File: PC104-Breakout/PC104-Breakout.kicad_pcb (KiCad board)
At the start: 4 copper layers, 175 x 100 mm, 20 parts, among them J1 Screw_Terminal_01x02, J2 Screw_Terminal_01x02, J3 Screw_Terminal_01x02, M1 MountingHole_Pad, M2 MountingHole_Pad, M3 MountingHole_Pad, M4 MountingHole_Pad, M5 MountingHole_Pad, M6 MountingHole_Pad, M7 MountingHole_Pad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

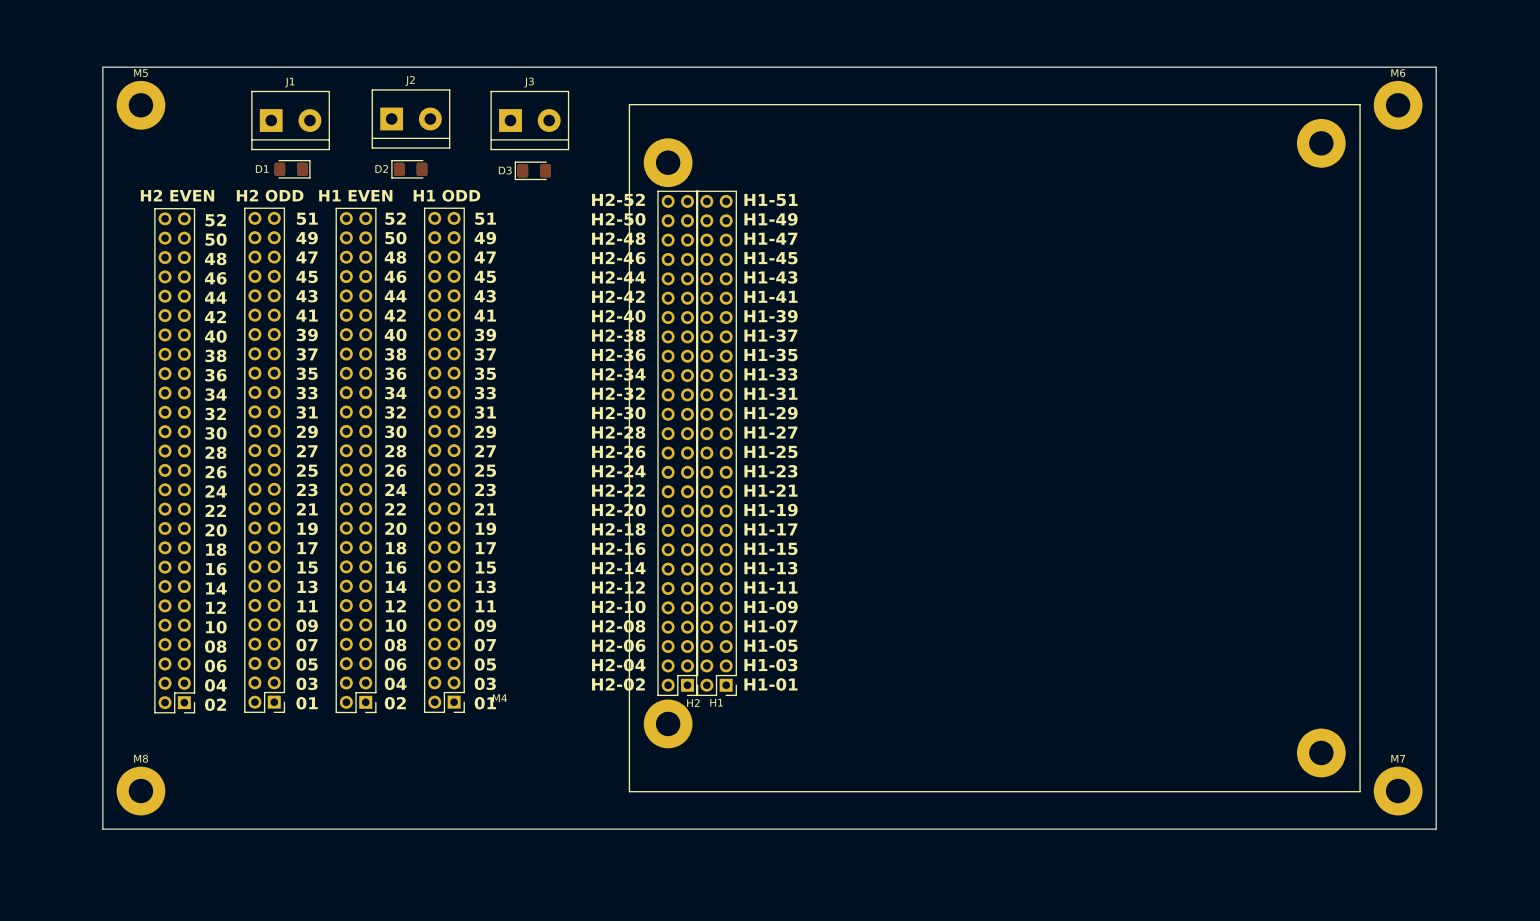
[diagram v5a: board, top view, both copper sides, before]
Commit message: semi final routing
- routed everything including power pins
- created GND, 3V3, and 5V pours
- added vias for diodes / routing

TODO: fix last two unrouted nets
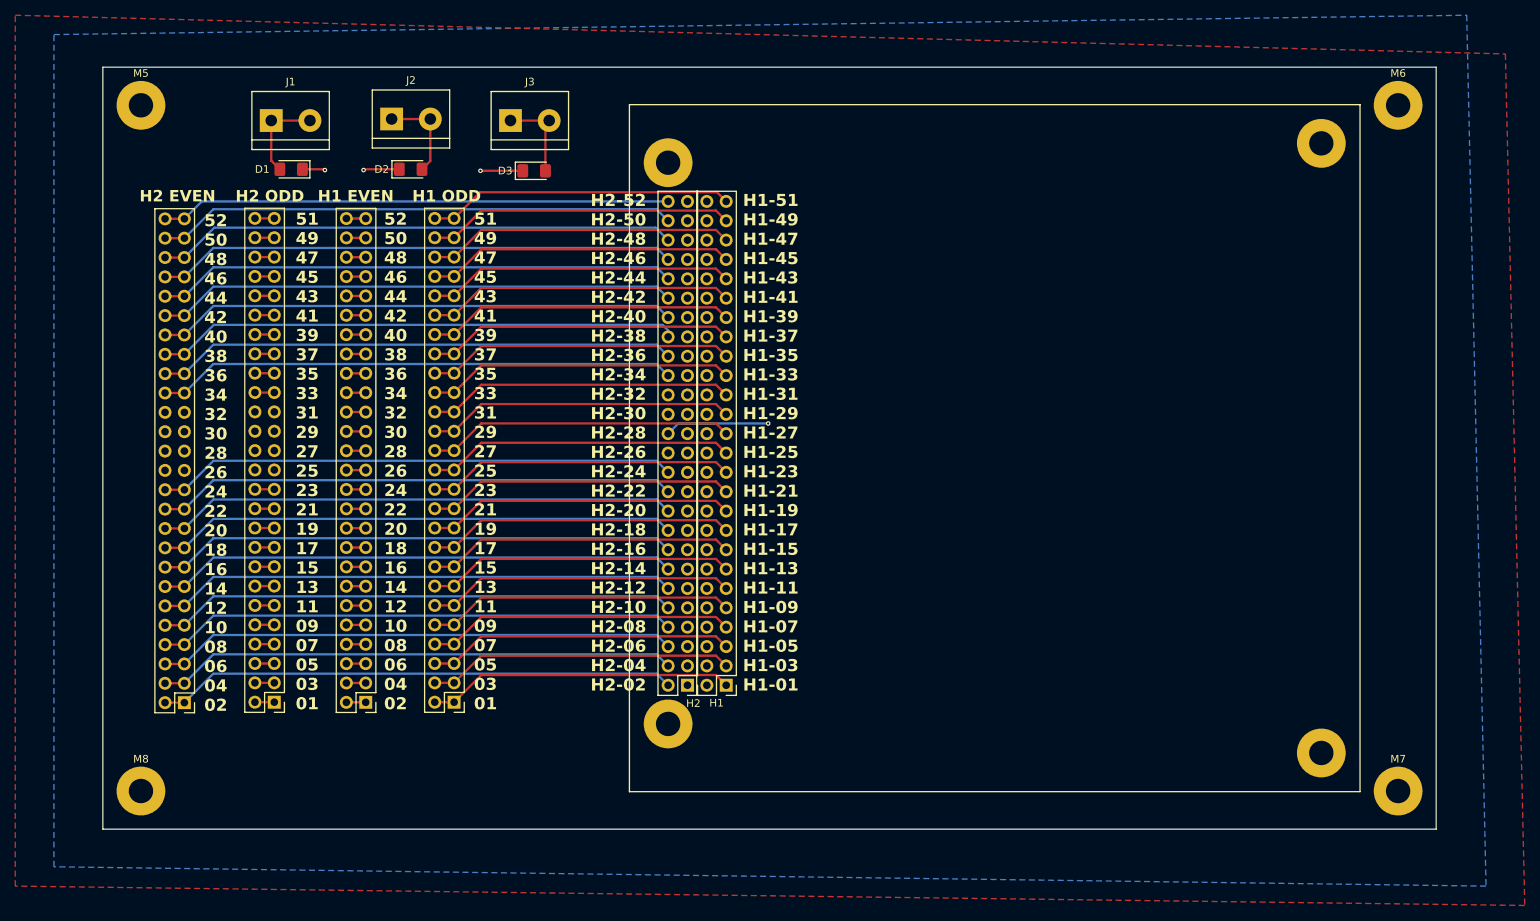
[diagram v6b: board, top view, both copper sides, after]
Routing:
- net H2-38: track 0.00 -> 68.8 mm
- net H2-48: track 0.00 -> 68.3 mm
- net H2-34: track 0.00 -> 68.2 mm
- net H2-20: track 0.00 -> 68.2 mm
- net H2-16: track 0.00 -> 68.2 mm
- net H2-02: track 0.00 -> 68.2 mm
- net H2-50: track 0.00 -> 68.2 mm
- net H2-46: track 0.00 -> 68.2 mm
- net H2-44: track 0.00 -> 68.2 mm
- net H2-42: track 0.00 -> 68.2 mm
- net H2-40: track 0.00 -> 68.2 mm
- net H2-36: track 0.00 -> 68.2 mm
- net H2-24: track 0.00 -> 68.2 mm
- net H2-22: track 0.00 -> 68.2 mm
- net H2-18: track 0.00 -> 68.2 mm
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- added copper zone on F.Cu, net H2-25
- added copper zone on In1.Cu, net H2-27
- added copper zone on B.Cu, net H2-29

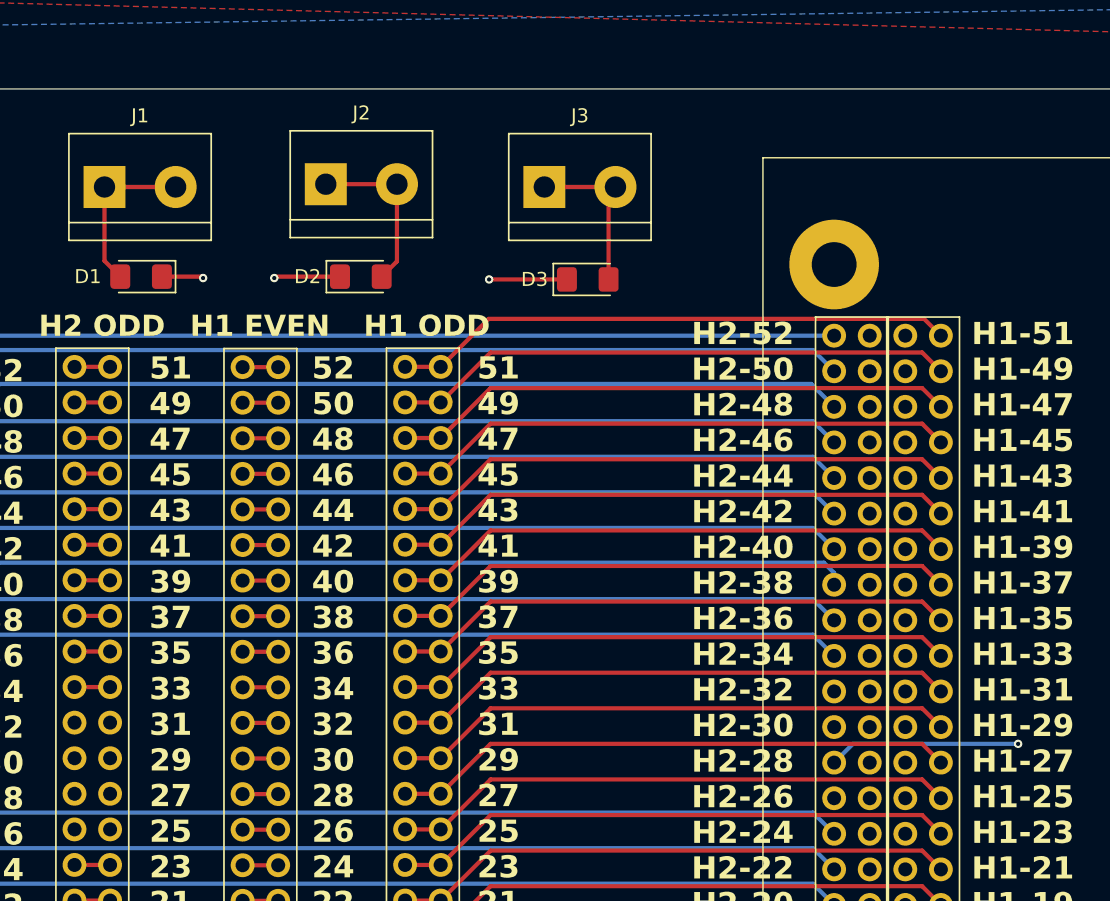
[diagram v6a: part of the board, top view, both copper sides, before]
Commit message: finished routing
- fixed final unrouted nets and vias
- silk screen edits
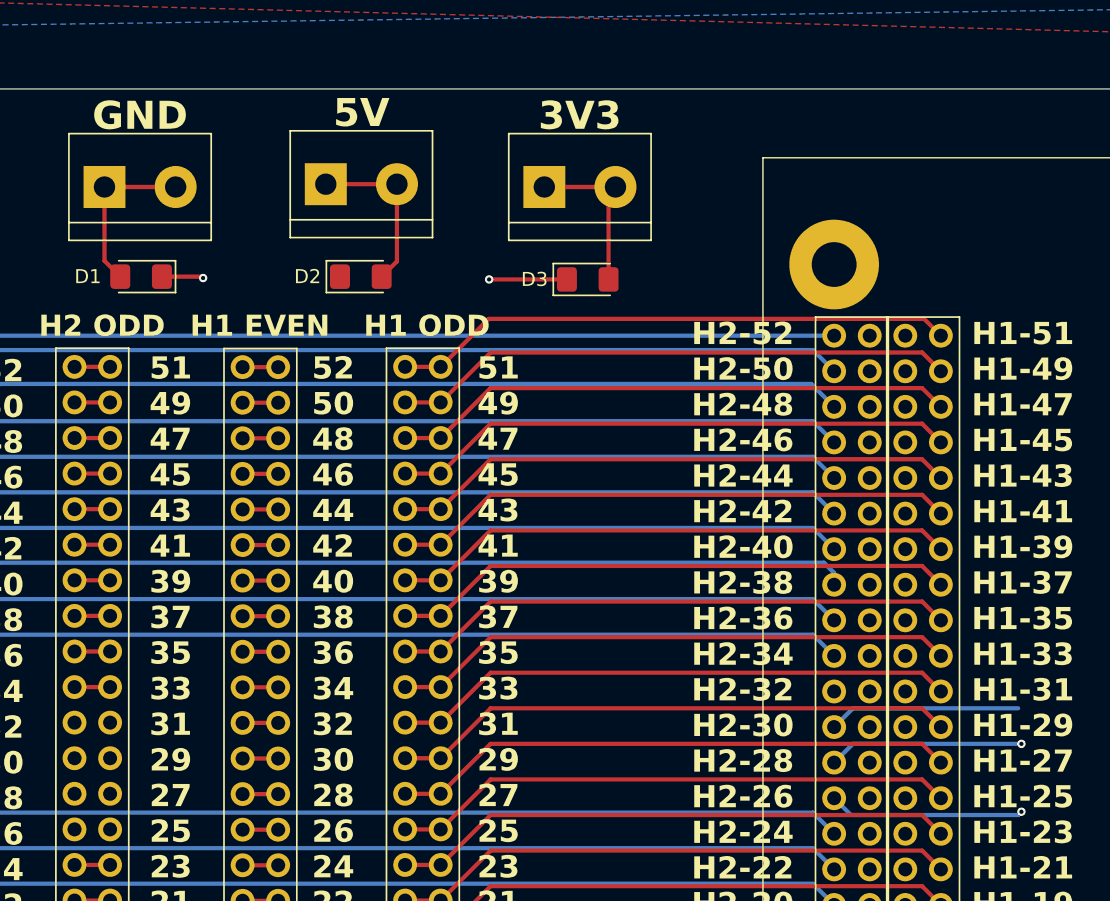
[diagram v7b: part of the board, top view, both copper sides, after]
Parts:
- renumbered J3 to 3V3, J2 to 5V, J1 to GND
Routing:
- net H2-29: track 3.15 -> 16.8 mm
- net H2-25: track 4.73 -> 14.0 mm
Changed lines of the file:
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@@
 		(descr "simple 2-pin terminal block, pitch 5.08mm, revamped version of bornier2")
 		(tags "terminal block bornier2")
-		(property "Reference" "J1"
+		(property "Reference" "GND"
 			(at 2.54 -5.08 0)
 			(layer "F.SilkS")
 			(effects
 				(font
-					(size 1 1)
-					(thickness 0.15)
+					(size 2 2)
+					(thickness 0.4)
+					(bold yes)
 				)
 			)
@@
 		(descr "simple 2-pin terminal block, pitch 5.08mm, revamped version of bornier2")
 		(tags "terminal block bornier2")
-		(property "Reference" "J3"
+		(property "Reference" "3V3"
 			(at 2.54 -5.08 0)
 			(layer "F.SilkS")
 			(effects
 				(font
-					(size 1 1)
-					(thickness 0.15)
+					(size 2 2)
+					(thickness 0.4)
+					(bold yes)
 				)
 			)
@@
 		(descr "simple 2-pin terminal block, pitch 5.08mm, revamped version of bornier2")
 		(tags "terminal block bornier2")
-		(property "Reference" "J2"
+		(property "Reference" "5V"
 			(at 2.54 -5.08 0)
 			(layer "F.SilkS")
 			(effects
 				(font
-					(size 1 1)
-					(thickness 0.15)
+					(size 2 2)
+					(thickness 0.4)
+					(bold yes)
 				)
 			)
@@
 		(net 55)
 	)
+	(via
+		(at 162.56 101.6)
+		(size 0.6)
+		(drill 0.3)
+		(layers "F.Cu" "B.Cu")
+		(net 56)
+	)
 	(segment
-		(start 113.9125 63.4)
-		(end 109.32 63.4)
+		(start 150.39 101.835)
+		(end 162.325 101.835)
 		(width 0.3)
-		(layer "F.Cu")
+		(layer "B.Cu")
 		(net 56)
 	)
 	(segment
-		(start 109.32 63.4)
-		(end 109.22 63.5)
+		(start 149.19 100.635)
+		(end 150.39 101.835)
 		(width 0.3)
-		(layer "F.Cu")
+		(layer "B.Cu")
 		(net 56)
 	)
-	(via
-		(at 109.22 63.5)
-		(size 0.6)
-		(drill 0.3)
-		(layers "F.Cu" "B.Cu")
+	(segment
+		(start 162.325 101.835)
+		(end 162.56 101.6)
+		(width 0.3)
+		(layer "B.Cu")
 		(net 56)
 	)
@@
 	)
 	(segment
+		(start 150.53 94.215)
+		(end 162.325 94.215)
+		(width 0.3)
+		(layer "B.Cu")
+		(net 58)
+	)
+	(segment
+		(start 149.19 95.555)
+		(end 150.53 94.215)
+		(width 0.3)
+		(layer "B.Cu")
+		(net 58)
+	)
+	(segment
 		(start 94.96 92.7)
 		(end 97.5 92.7)
@@
 	)
 	(via
-		(at 162.325 96.755)
+		(at 162.56 96.755)
 		(size 0.6)
 		(drill 0.3)
@@
 	)
 	(segment
-		(start 162.325 96.755)
+		(start 149.19 98.095)
 		(end 150.53 96.755)
 		(width 0.3)
@@
 	(segment
 		(start 150.53 96.755)
-		(end 149.19 98.095)
+		(end 162.56 96.755)
 		(width 0.3)
 		(layer "B.Cu")

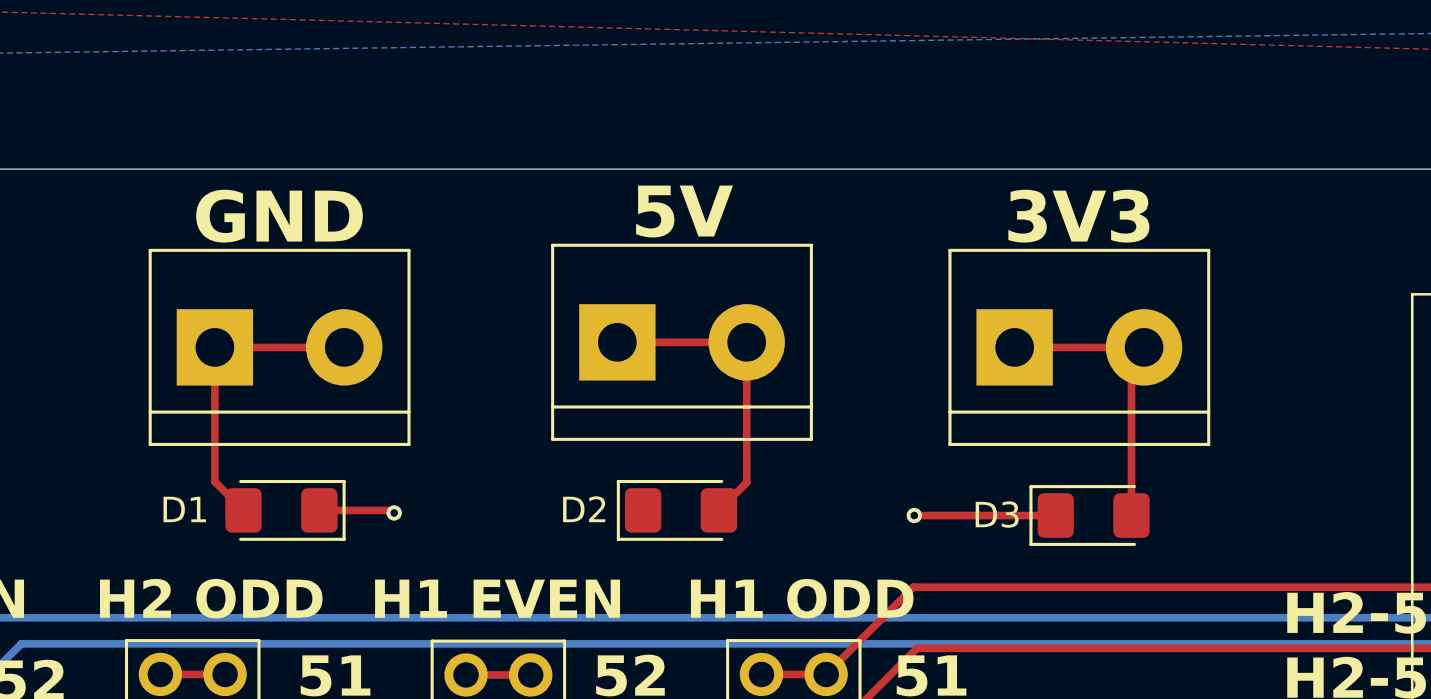
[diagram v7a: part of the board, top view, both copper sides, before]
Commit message: Fixed LED orientations and finalized board design
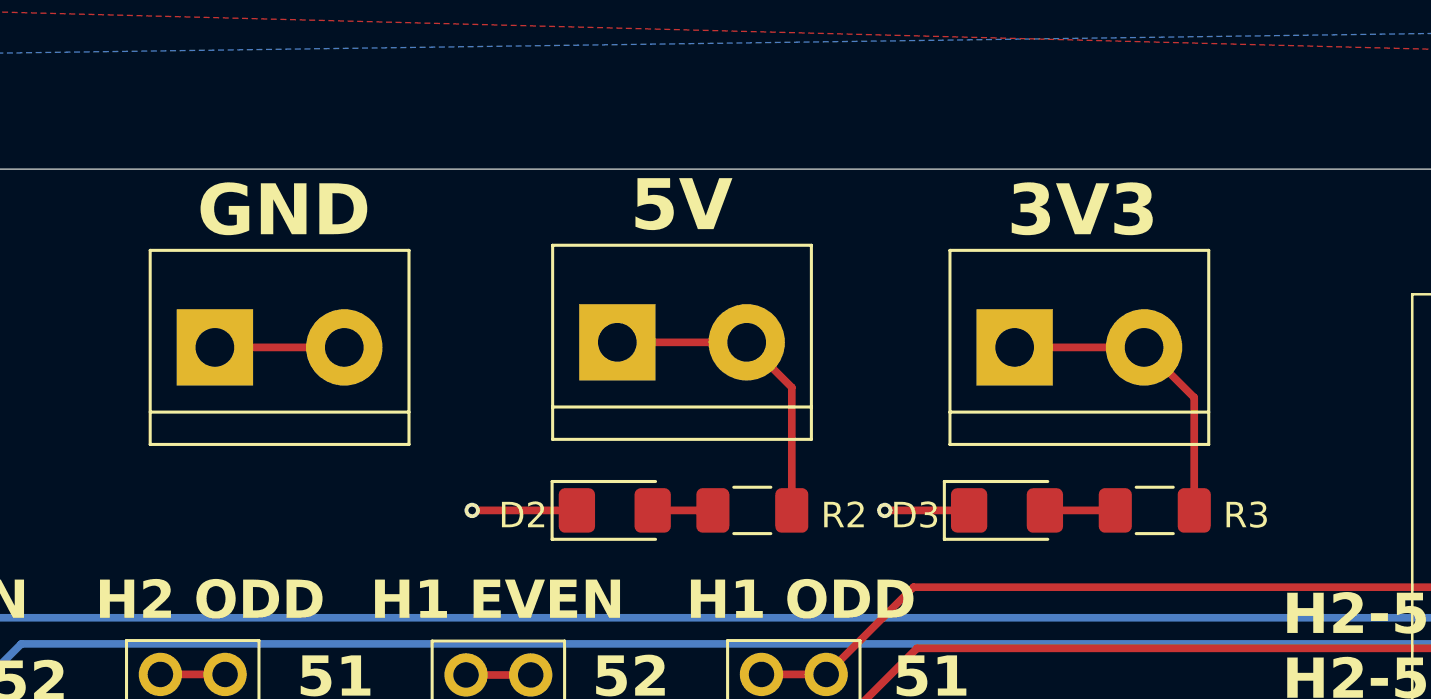
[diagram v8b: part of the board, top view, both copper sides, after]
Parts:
- removed D1: D, Diode_SMD:D_1206_3216Metric_Pad1.42x1.75mm_HandSolder
- added R2: 3.3k, Resistor_SMD:R_1206_3216Metric_Pad1.30x1.75mm_HandSolder, F.Cu at (118.2, 63.4)
- added R3: 2.2k, Resistor_SMD:R_1206_3216Metric_Pad1.30x1.75mm_HandSolder, F.Cu at (134.0, 63.4)
- moved D3 3.41 mm to (128.2, 63.4)
- moved D2 2.60 mm to (112.8, 63.4)
- renumbered GND to J1, 5V to J2, 3V3 to J3
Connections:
- D2 pad 1: H2-25 -> H2-29
- D3 pad 1: H2-27 -> H2-29
- J1 pad 1: Net-(D1-A) -> H2-29
- J1 pad 2: Net-(D1-A) -> H2-29
- J2 pad 1: Net-(D2-A) -> H2-25
- J2 pad 2: Net-(D2-A) -> H2-25
- J3 pad 1: Net-(D3-A) -> H2-27
- J3 pad 2: Net-(D3-A) -> H2-27
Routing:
- net H2-25: track 14.0 -> 26.4 mm
- net Net-(D1-A): track 11.9 -> 0.00 mm
- net Net-(D2-A): track 12.1 -> 2.36 mm
- net H2-29: track 16.8 -> 26.4 mm, vias 1 -> 2
- net Net-(D3-A): track 11.9 -> 2.76 mm
- net H2-27: track 19.6 -> 27.3 mm, vias 2 -> 1
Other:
- board text added: "3V3"
- board text added: "5V"
- board text added: "GND"
